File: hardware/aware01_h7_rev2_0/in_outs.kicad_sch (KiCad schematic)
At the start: 32 parts, among them J4 InL, J5 InR, J6 OutL, J7 OutR, U10 NE5532DRG4, U9 NE5532DRG4

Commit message: add 5V buck converter
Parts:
- J4, J5, J6, J7: footprint Connector_Audio:Jack_3.5mm_QingPu_WQP-PJ398SM_Vertical_CircularHoles -> AudioJacks:Jack_3.5mm_QingPu_WQP-PJ398SM_Vertical
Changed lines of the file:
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@@
 			)
 		)
-		(property "Footprint" "Connector_Audio:Jack_3.5mm_QingPu_WQP-PJ398SM_Vertical_CircularHoles"
+		(property "Footprint" "AudioJacks:Jack_3.5mm_QingPu_WQP-PJ398SM_Vertical"
 			(at 247.65 67.31 0)
 			(effects
@@
 			)
 		)
-		(property "Footprint" "Connector_Audio:Jack_3.5mm_QingPu_WQP-PJ398SM_Vertical_CircularHoles"
+		(property "Footprint" "AudioJacks:Jack_3.5mm_QingPu_WQP-PJ398SM_Vertical"
 			(at 41.91 62.23 0)
 			(effects
@@
 			)
 		)
-		(property "Footprint" "Connector_Audio:Jack_3.5mm_QingPu_WQP-PJ398SM_Vertical_CircularHoles"
+		(property "Footprint" "AudioJacks:Jack_3.5mm_QingPu_WQP-PJ398SM_Vertical"
 			(at 247.65 135.89 0)
 			(effects
@@
 			)
 		)
-		(property "Footprint" "Connector_Audio:Jack_3.5mm_QingPu_WQP-PJ398SM_Vertical_CircularHoles"
+		(property "Footprint" "AudioJacks:Jack_3.5mm_QingPu_WQP-PJ398SM_Vertical"
 			(at 41.91 130.81 0)
 			(effects

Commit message: schematic formatting
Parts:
- J4, J5, J6, J7: now left out of the parts list
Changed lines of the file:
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@@
 		(unit 1)
 		(exclude_from_sim no)
-		(in_bom yes)
+		(in_bom no)
 		(on_board yes)
 		(dnp no)
@@
 		(unit 1)
 		(exclude_from_sim no)
-		(in_bom yes)
+		(in_bom no)
 		(on_board yes)
 		(dnp no)
@@
 		(unit 1)
 		(exclude_from_sim no)
-		(in_bom yes)
+		(in_bom no)
 		(on_board yes)
 		(dnp no)
@@
 		(unit 1)
 		(exclude_from_sim no)
-		(in_bom yes)
-		(on_board yes)
-		(dnp no)
+		(in_bom no)
+		(on_board yes)
+		(dnp no)

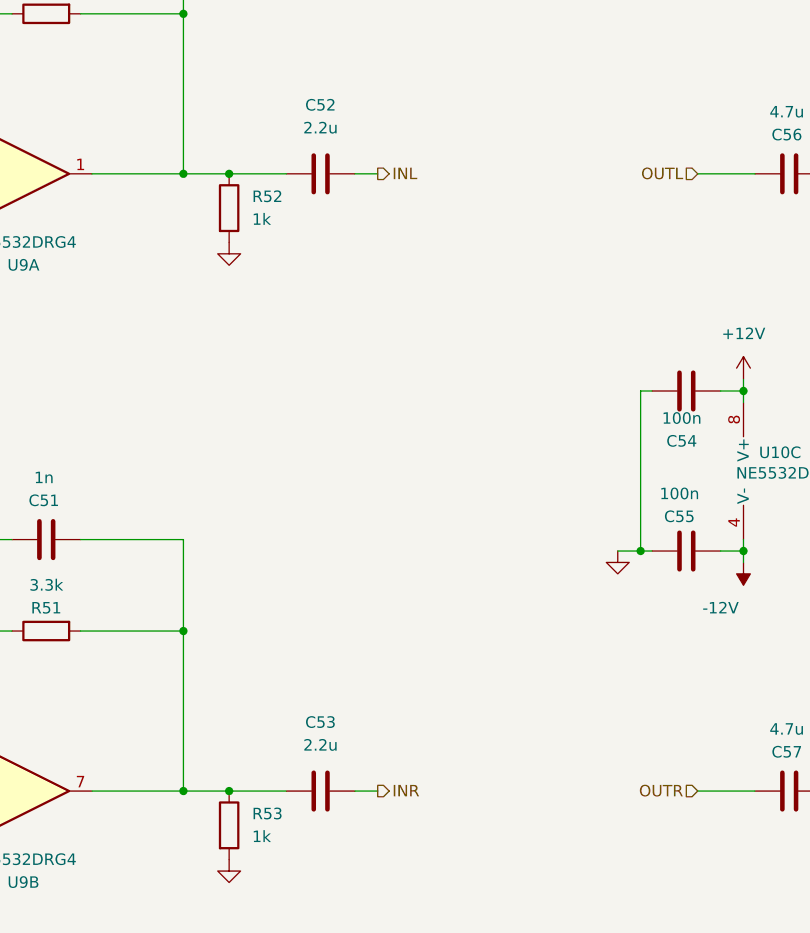
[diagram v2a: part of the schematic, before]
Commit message: refine layout, add testpoints
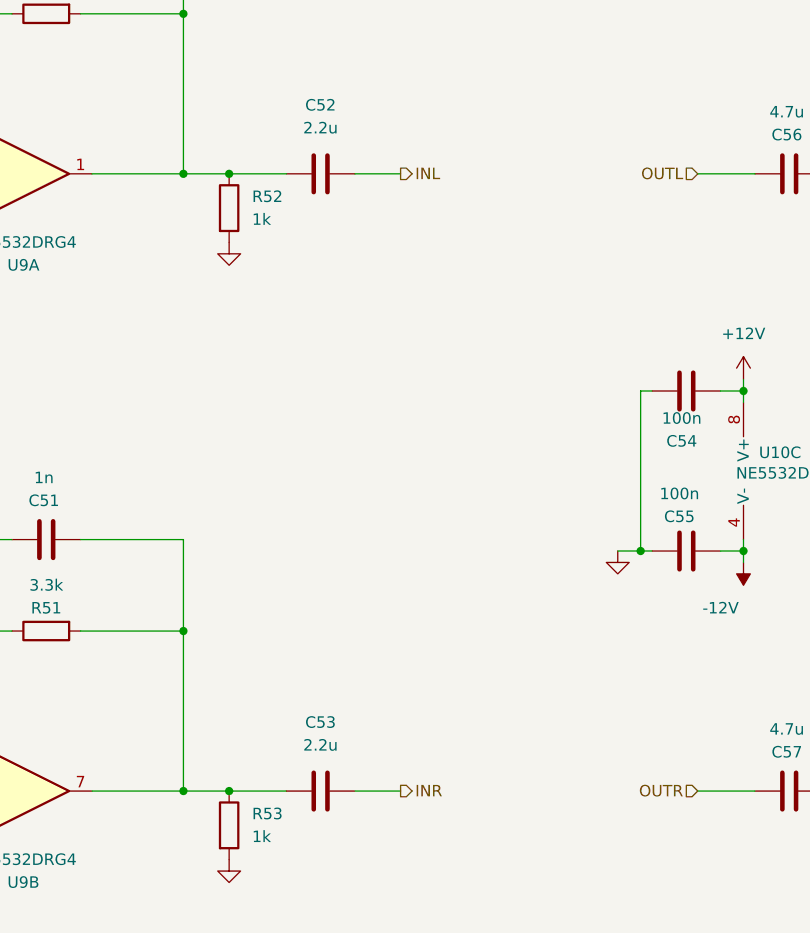
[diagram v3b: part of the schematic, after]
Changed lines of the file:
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@@
 	(wire
 		(pts
-			(xy 125.73 64.77) (xy 128.27 64.77)
+			(xy 125.73 64.77) (xy 130.81 64.77)
 		)
 		(stroke
@@
 	(wire
 		(pts
-			(xy 125.73 133.35) (xy 128.27 133.35)
+			(xy 125.73 133.35) (xy 130.81 133.35)
 		)
 		(stroke
@@
 	(hierarchical_label "INL"
 		(shape output)
-		(at 128.27 64.77 0)
+		(at 130.81 64.77 0)
 		(effects
 			(font
@@
 	(hierarchical_label "INR"
 		(shape output)
-		(at 128.27 133.35 0)
+		(at 130.81 133.35 0)
 		(effects
 			(font

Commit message: hw: update hw design
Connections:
- net GND: now also J4.TN
- no-connect marks 3 -> 2
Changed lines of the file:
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@@
+	)
+	(junction
+		(at 49.53 64.77)
+		(diameter 0)
+		(color 0 0 0 0)
 	)
 	(junction
@@
 	)
 	(no_connect
-		(at 46.99 59.69)
-	)
-	(no_connect
 		(at 242.57 64.77)
 	)
@@
 	(wire
 		(pts
+			(xy 49.53 59.69) (xy 49.53 64.77)
+		)
+		(stroke
+			(width 0)
+			(type default)
+		)
+	)
+	(wire
+		(pts
 			(xy 106.68 133.35) (xy 111.76 133.35)
 		)
@@
 		)
 		(stroke
+			(width 0)
+			(type default)
+		)
+	)
+	(wire
+		(pts
+			(xy 46.99 59.69) (xy 49.53 59.69)
+		)
+		(stroke

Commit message: hardware: update analog sim and routing (wip)
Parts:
- removed C50, C51: 1n, Capacitor_SMD:C_0603_1608Metric, symbol Device:C
- removed C53: 2.2u, Capacitor_SMD:CP_Elec_4x5.4, symbol Device:C
- removed C56, C57: 4.7u, Capacitor_SMD:CP_Elec_4x5.4, symbol Device:C
- removed C58, C59: 220p, Capacitor_SMD:C_0603_1608Metric, symbol Device:C
- removed R48, R49, R58, R59: 22k, Resistor_SMD:R_0603_1608Metric_Pad0.98x0.95mm_HandSolder, symbol Device:R
- removed R50, R51, R56, R57: 3.3k, Resistor_SMD:R_0603_1608Metric_Pad0.98x0.95mm_HandSolder, symbol Device:R
- removed R52, R53, R60, R61: 1k, Resistor_SMD:R_0603_1608Metric_Pad0.98x0.95mm_HandSolder, symbol Device:R
- removed R54, R55: 100k, Resistor_SMD:R_0603_1608Metric_Pad0.98x0.95mm_HandSolder, symbol Device:R
- added C49: 2.2u, Capacitor_SMD:CP_Elec_4x5.4, symbol Device:C_Polarized
- added C52, C53: 10u, Capacitor_SMD:CP_Elec_4x5.4, symbol Device:C_Polarized
- added C54, C55: 18p, Capacitor_SMD:C_0603_1608Metric, symbol Device:C
- added D4, D5: BAT54S, Package_TO_SOT_SMD:SOT-23, symbol Diode:BAT54S
- added R14, R15: 12k, Resistor_SMD:R_0603_1608Metric_Pad0.98x0.95mm_HandSolder, symbol Device:R
- added R16, R17: 1.8k, Resistor_SMD:R_0603_1608Metric_Pad0.98x0.95mm_HandSolder, symbol Device:R
- added R18, R19: 5.6k, Resistor_SMD:R_0603_1608Metric_Pad0.98x0.95mm_HandSolder, symbol Device:R
- added R20, R21: 39k, Resistor_SMD:R_0603_1608Metric_Pad0.98x0.95mm_HandSolder, symbol Device:R
- added R22, R23: 1k, Resistor_SMD:R_0603_1608Metric_Pad0.98x0.95mm_HandSolder, symbol Device:R
- C48: renamed from C52; symbol Device:C -> Device:C_Polarized
- renumbered C48 to C46, C49 to C47, C54 to C50, C55 to C51, J4 to J3, J5 to J4, J6 to J5, J7 to J6, U9 to U10, U10 to U11
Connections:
- net GND: now also D4.2 (K), D5.2 (K), R16.1, R17.1; no longer U10.3 (+), U10.5 (+)
- net INL: now also C48.1, D4.3 (COM); no longer C48.2
- net INR: now also C49.1, D5.3 (COM)
- net OUTL: now also C52.1
- net OUTR: now also C53.1
- net at U10.1: now also U10.2 (-), R14.1; no longer C48.1
- net at U10.7: now also U10.6 (-), R15.1
- net at U11.6 (-): now also C55.1, R19.2, R21.1
- net at U11.7: now also C55.2, R21.2, R23.1
- net at J5.T: now also R22.2
- net at J3.T, J4.TN: now also U10.3 (+)
- net at U11.2 (-): now also C54.1, R18.2, R20.1
- net at U11.1: now also C54.2, R20.2, R22.1
- net at J6.T: now also R23.2
- net at J4.T: now also U10.5 (+)
- new net: C49.2, R15.2, R17.2
- new net: C48.2, R14.2, R16.2
- new net: C52.2, R18.1
- new net: C53.2, R19.1
- new net +1V8: D4.1 (A), D5.1 (A)
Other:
- moved on the sheet: J5, J6, U10A, U10B, U11A, U11B

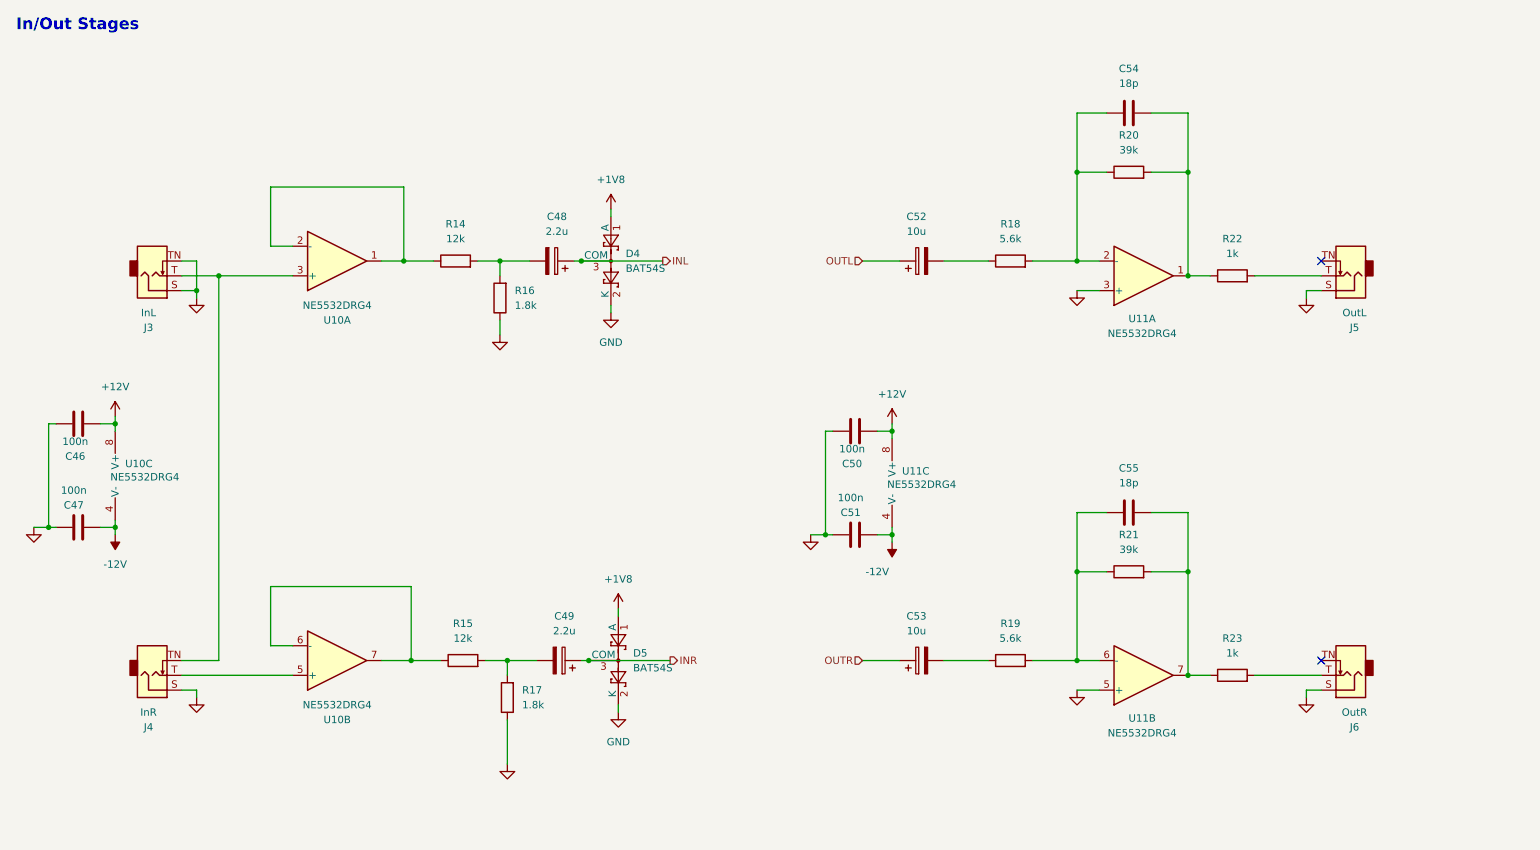
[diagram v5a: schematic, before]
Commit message: hardware: update layout
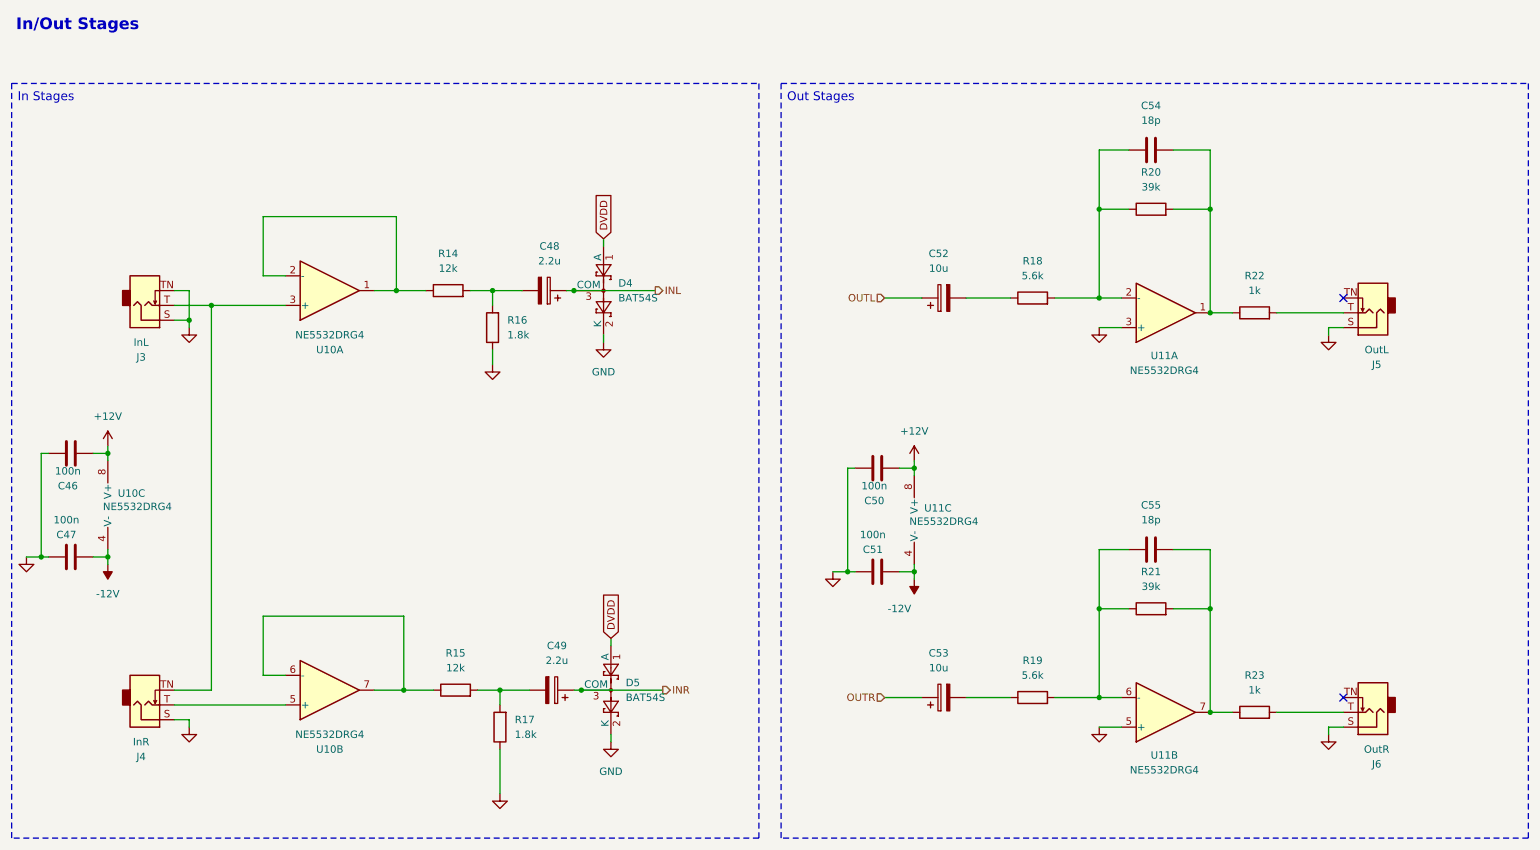
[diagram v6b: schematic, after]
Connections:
- net +1V8 renamed DVDD
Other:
- note added: "In Stages"
- note added: "Out Stages"
- company: (none) -> Ausschussware
- title: (none) -> Aware 01 - Eurorack DSP Module
- moved on the sheet: C46, C47, C48, C49, C50, C51, C52, C53, C54, C55, D4, D5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

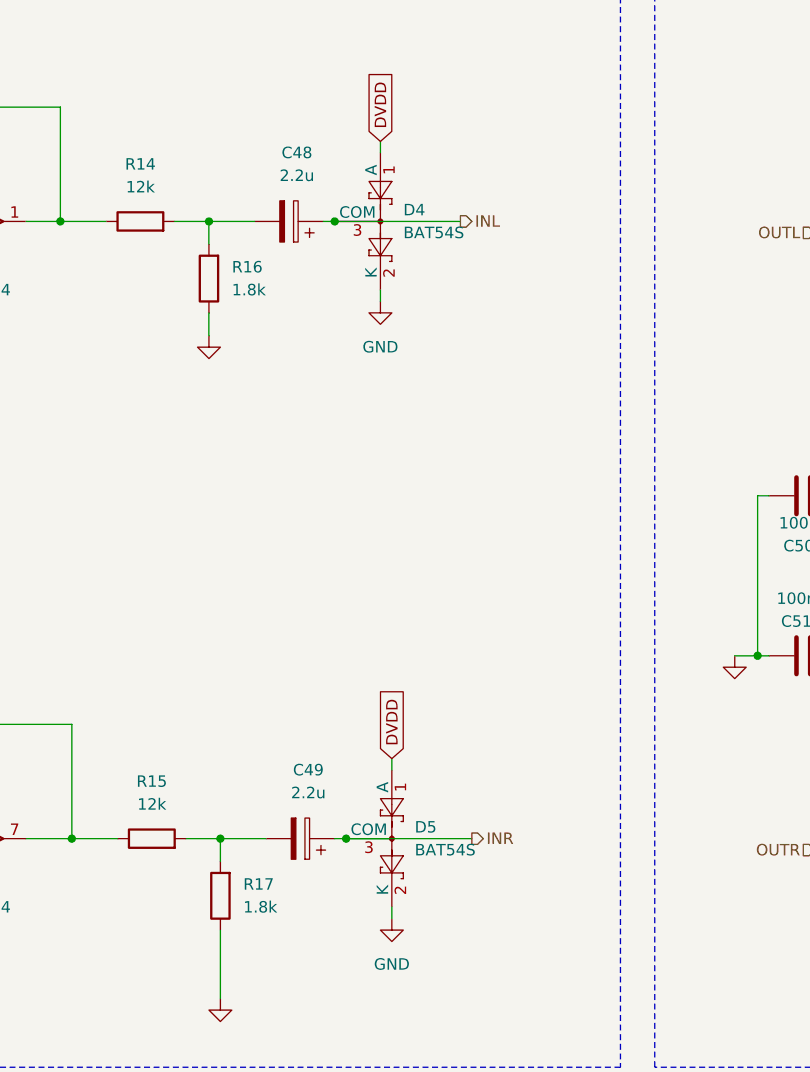
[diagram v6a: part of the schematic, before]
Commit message: hardware: fix clamping diode orientation
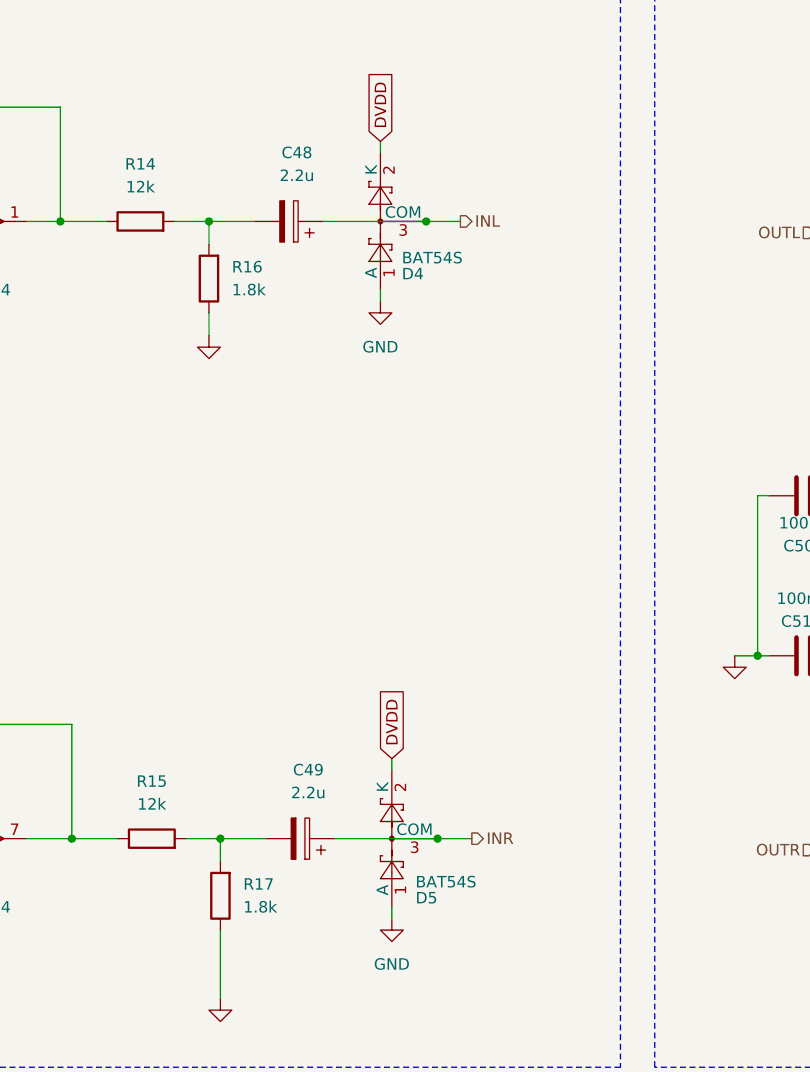
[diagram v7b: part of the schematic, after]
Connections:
- net DVDD: now also D4.2 (K), D5.2 (K); no longer D4.1 (A), D5.1 (A)
- net GND: now also D4.1 (A), D5.1 (A); no longer D4.2 (K), D5.2 (K)
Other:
- moved on the sheet: D4, D5
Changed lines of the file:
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@@
 	)
 	(junction
+		(at 124.46 64.77)
+		(diameter 0)
+		(color 0 0 0 0)
+	)
+	(junction
 		(at 204.47 66.04)
 		(diameter 0)
@@
 	)
 	(junction
-		(at 115.57 133.35)
+		(at 34.29 110.49)
 		(diameter 0)
 		(color 0 0 0 0)
 	)
 	(junction
-		(at 34.29 110.49)
+		(at 125.73 133.35)
 		(diameter 0)
 		(color 0 0 0 0)
@@
 	)
 	(junction
-		(at 114.3 64.77)
-		(diameter 0)
-		(color 0 0 0 0)
-	)
-	(junction
 		(at 161.29 113.03)
 		(diameter 0)
@@
 	(wire
 		(pts
-			(xy 114.3 64.77) (xy 128.27 64.77)
-		)
-		(stroke
-			(width 0)
-			(type default)
-		)
-	)
-	(wire
-		(pts
 			(xy 31.75 110.49) (xy 34.29 110.49)
 		)
@@
 	(wire
 		(pts
-			(xy 115.57 133.35) (xy 129.54 133.35)
-		)
-		(stroke
-			(width 0)
-			(type default)
-		)
-	)
-	(wire
-		(pts
 			(xy 246.38 71.12) (xy 243.84 71.12)
 		)
@@
 	(wire
 		(pts
-			(xy 113.03 64.77) (xy 114.3 64.77)
+			(xy 113.03 64.77) (xy 124.46 64.77)
 		)
 		(stroke
@@
 	(wire
 		(pts
+			(xy 124.46 64.77) (xy 128.27 64.77)
+		)
+		(stroke
+			(width 0)
+			(type default)
+		)
+	)
+	(wire
+		(pts
 			(xy 45.72 135.89) (xy 64.77 135.89)
 		)
@@
 	(wire
 		(pts
-			(xy 114.3 133.35) (xy 115.57 133.35)
+			(xy 114.3 133.35) (xy 125.73 133.35)
 		)
 		(stroke
@@
 	(wire
 		(pts
+			(xy 125.73 133.35) (xy 129.54 133.35)
+		)
+		(stroke
+			(width 0)
+			(type default)
+		)
+	)
+	(wire
+		(pts
 			(xy 172.72 93.98) (xy 172.72 95.25)
 		)
@@
 	(symbol
 		(lib_id "Diode:BAT54S")
-		(at 119.38 64.77 270)
+		(at 119.38 64.77 90)
 		(unit 1)
 		(exclude_from_sim no)
@@
 		(on_board yes)
 		(dnp no)
-		(fields_autoplaced yes)
 		(property "Reference" "D4"
-			(at 121.92 63.4999 90)
+			(at 124.206 70.612 90)
 			(effects
 				(font
@@
 		)
 		(property "Value" "BAT54S"
-			(at 121.92 66.0399 90)
+			(at 128.524 68.834 90)
 			(effects
 				(font
@@
 		)
 		(property "Footprint" "Package_TO_SOT_SMD:SOT-23"
-			(at 122.555 66.675 0)
+			(at 116.205 62.865 0)
 			(effects
 				(font
@@
 		)
 		(property "Datasheet" "https://www.diodes.com/assets/Datasheets/ds11005.pdf"
-			(at 119.38 61.722 0)
+			(at 119.38 67.818 0)
 			(effects
 				(font
@@
 	(symbol
 		(lib_id "Diode:BAT54S")
-		(at 120.65 133.35 270)
+		(at 120.65 133.35 90)
 		(unit 1)
 		(exclude_from_sim no)
@@
 		(on_board yes)
 		(dnp no)
-		(fields_autoplaced yes)
 		(property "Reference" "D5"
-			(at 123.19 132.0799 90)
+			(at 125.73 139.954 90)
 			(effects
 				(font
@@
 		)
 		(property "Value" "BAT54S"
-			(at 123.19 134.6199 90)
+			(at 130.048 138.176 90)
 			(effects
 				(font
@@
 		)
 		(property "Footprint" "Package_TO_SOT_SMD:SOT-23"
-			(at 123.825 135.255 0)
+			(at 117.475 131.445 0)
 			(effects
 				(font
@@
 		)
 		(property "Datasheet" "https://www.diodes.com/assets/Datasheets/ds11005.pdf"
-			(at 120.65 130.302 0)
+			(at 120.65 136.398 0)
 			(effects
 				(font
